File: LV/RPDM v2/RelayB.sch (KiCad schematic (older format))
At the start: 6 parts, among them K2 G8NW, Q2 Q_Dual_NMOS

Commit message: rPDM - Started on board layout
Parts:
- D6, D7: renamed from D?; footprint (none) -> Diode_UOWM:TO-277_FSV10150V
- gave numbers to parts that had none: 2
- renumbered K2 to K3, Q2 to Q3
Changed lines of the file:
@@
 $EndDescr
 $Comp
-L Device2:Q_Dual_NMOS_S1G1S2G2D2D2D1D1 Q2
+L Device2:Q_Dual_NMOS_S1G1S2G2D2D2D1D1 Q3
 U 2 1 6114EE63
 P 5900 4500
-AR Path="/5E554D5D/60DE88EB/6114EE63" Ref="Q2"  Part="2"
-AR Path="/5E554D5D/60DEDCB5/6114EE63" Ref="Q1"  Part="2"
-F 0 "Q2" H 6188 4546 50  0000 L CNN
+AR Path="/5E554D5D/60DE88EB/6114EE63" Ref="Q3"  Part="2"
+AR Path="/5E554D5D/60DEDCB5/6114EE63" Ref="Q2"  Part="2"
+F 0 "Q3" H 6188 4546 50  0000 L CNN
 F 1 "Q_Dual_NMOS" H 6188 4455 50  0000 L CNN
 F 2 "" H 6100 4500 50  0001 C CNN
@@
 $EndComp
 $Comp
-L relay_omron:G8NW K2
+L relay_omron:G8NW K3
 U 2 1 61727FFD
 P 5500 3300
-AR Path="/5E554D5D/60DE88EB/61727FFD" Ref="K2"  Part="2"
-AR Path="/5E554D5D/60DEDCB5/61727FFD" Ref="K1"  Part="2"
-F 0 "K2" V 6081 3300 50  0000 C CNN
+AR Path="/5E554D5D/60DE88EB/61727FFD" Ref="K3"  Part="2"
+AR Path="/5E554D5D/60DEDCB5/61727FFD" Ref="K2"  Part="2"
+F 0 "K3" V 6081 3300 50  0000 C CNN
 F 1 "G8NW" V 5990 3300 50  0000 C CNN
 F 2 "" H 5900 3200 50  0001 L CNN
@@
 AR Path="/5E554D5D/60DE7B67/617E89A2" Ref="#PWR?"  Part="1"
 AR Path="/5E554D5D/60DE7FBD/617E89A2" Ref="#PWR?"  Part="1"
-AR Path="/5E554D5D/60DE88EB/617E89A2" Ref="#PWR?"  Part="1"
+AR Path="/5E554D5D/60DE88EB/617E89A2" Ref="#PWR023"  Part="1"
 AR Path="/5E554D5D/60DED789/617E89A2" Ref="#PWR?"  Part="1"
-AR Path="/5E554D5D/60DEDCB5/617E89A2" Ref="#PWR?"  Part="1"
+AR Path="/5E554D5D/60DEDCB5/617E89A2" Ref="#PWR017"  Part="1"
 AR Path="/60E5EBEF/617E89A2" Ref="#PWR?"  Part="1"
-F 0 "#PWR?" H 6000 4750 50  0001 C CNN
+F 0 "#PWR023" H 6000 4750 50  0001 C CNN
 F 1 "GND" H 6005 4827 50  0000 C CNN
 F 2 "" H 6000 5000 50  0001 C CNN
@@
 AR Path="/5E554D5D/5E5E9CA9/617E89AB" Ref="R?"  Part="1"
 AR Path="/5E554D5D/60DED789/617E89AB" Ref="R?"  Part="1"
-AR Path="/5E554D5D/60DE88EB/617E89AB" Ref="R?"  Part="1"
-AR Path="/5E554D5D/60DEDCB5/617E89AB" Ref="R?"  Part="1"
-F 0 "R?" H 5070 4796 50  0000 L CNN
+AR Path="/5E554D5D/60DE88EB/617E89AB" Ref="R16"  Part="1"
+AR Path="/5E554D5D/60DEDCB5/617E89AB" Ref="R12"  Part="1"
+F 0 "R16" H 5070 4796 50  0000 L CNN
 F 1 "100k" H 5070 4705 50  0000 L CNN
 F 2 "Resistor_SMD:R_0805_2012Metric_Pad1.15x1.40mm_HandSolder" V 4930 4750 50  0001 C CNN
@@
 AR Path="/5E554D5D/60DE7B67/617E89B2" Ref="#PWR?"  Part="1"
 AR Path="/5E554D5D/60DE7FBD/617E89B2" Ref="#PWR?"  Part="1"
-AR Path="/5E554D5D/60DE88EB/617E89B2" Ref="#PWR?"  Part="1"
+AR Path="/5E554D5D/60DE88EB/617E89B2" Ref="#PWR022"  Part="1"
 AR Path="/5E554D5D/60DED789/617E89B2" Ref="#PWR?"  Part="1"
-AR Path="/5E554D5D/60DEDCB5/617E89B2" Ref="#PWR?"  Part="1"
+AR Path="/5E554D5D/60DEDCB5/617E89B2" Ref="#PWR016"  Part="1"
 AR Path="/60E5EBEF/617E89B2" Ref="#PWR?"  Part="1"
-F 0 "#PWR?" H 5000 4750 50  0001 C CNN
+F 0 "#PWR022" H 5000 4750 50  0001 C CNN
 F 1 "GND" H 5005 4827 50  0000 C CNN
 F 2 "" H 5000 5000 50  0001 C CNN
@@
 AR Path="/5E554D5D/5E5E9CA9/617E89C5" Ref="R?"  Part="1"
 AR Path="/5E554D5D/60DED789/617E89C5" Ref="R?"  Part="1"
-F 0 "R?" V 5293 4500 50  0000 C CNN
+AR Path="/5E554D5D/60DEDCB5/617E89C5" Ref="R13"  Part="1"
+AR Path="/5E554D5D/60DE88EB/617E89C5" Ref="R17"  Part="1"
+F 0 "R17" V 5293 4500 50  0000 C CNN
 F 1 "470" V 5384 4500 50  0000 C CNN
 F 2 "Resistor_SMD:R_0805_2012Metric_Pad1.15x1.40mm_HandSolder" V 5430 4500 50  0001 C CNN
@@
 AR Path="/5E554D5D/60DE7B67/617E89CB" Ref="#PWR?"  Part="1"
 AR Path="/5E554D5D/60DE7FBD/617E89CB" Ref="#PWR?"  Part="1"
-AR Path="/5E554D5D/60DE88EB/617E89CB" Ref="#PWR?"  Part="1"
+AR Path="/5E554D5D/60DE88EB/617E89CB" Ref="#PWR024"  Part="1"
 AR Path="/5E554D5D/60DED789/617E89CB" Ref="#PWR?"  Part="1"
-AR Path="/5E554D5D/60DEDCB5/617E89CB" Ref="#PWR?"  Part="1"
+AR Path="/5E554D5D/60DEDCB5/617E89CB" Ref="#PWR018"  Part="1"
 AR Path="/60E5EBEF/617E89CB" Ref="#PWR?"  Part="1"
-F 0 "#PWR?" H 6500 3750 50  0001 C CNN
+F 0 "#PWR024" H 6500 3750 50  0001 C CNN
 F 1 "GND" H 6505 3827 50  0000 C CNN
 F 2 "" H 6500 4000 50  0001 C CNN
@@
 AR Path="/5E554D5D/60DED789/617E89D1" Ref="D?"  Part="1"
 AR Path="/5E554D5D/5E5E9CA9/617E89D1" Ref="D?"  Part="1"
-F 0 "D?" H 5500 4100 50  0000 C CNN
+AR Path="/5E554D5D/60DEDCB5/617E89D1" Ref="D6"  Part="1"
+AR Path="/5E554D5D/60DE88EB/617E89D1" Ref="D10"  Part="1"
+F 0 "D10" H 5500 4100 50  0000 C CNN
 F 1 "D_Schottky_Flyback" H 5450 3900 50  0000 C CNN
-F 2 "" H 5500 4000 50  0001 C CNN
+F 2 "Diode_UOWM:TO-277_FSV10150V" H 5500 4000 50  0001 C CNN
 F 3 "~" H 5500 4000 50  0001 C CNN
 	1    5500 4000
@@
 AR Path="/5E554D5D/60DED789/617E89D7" Ref="D?"  Part="1"
 AR Path="/5E554D5D/5E5E9CA9/617E89D7" Ref="D?"  Part="1"
-F 0 "D?" V 6479 3644 50  0000 L CNN
+AR Path="/5E554D5D/60DEDCB5/617E89D7" Ref="D7"  Part="1"
+AR Path="/5E554D5D/60DE88EB/617E89D7" Ref="D11"  Part="1"
+F 0 "D11" V 6479 3644 50  0000 L CNN
 F 1 "D_Schottky_Flyback" V 6570 3644 50  0000 L CNN
-F 2 "" H 6500 3500 50  0001 C CNN
+F 2 "Diode_UOWM:TO-277_FSV10150V" H 6500 3500 50  0001 C CNN
 F 3 "~" H 6500 3500 50  0001 C CNN
 	1    6500 3500

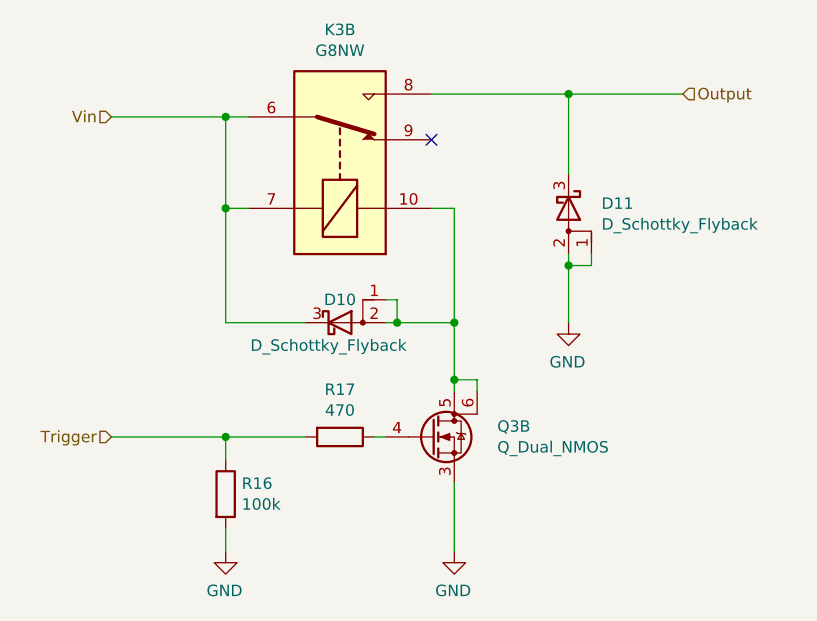
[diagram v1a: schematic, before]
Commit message: rpdm, libraries cleanup
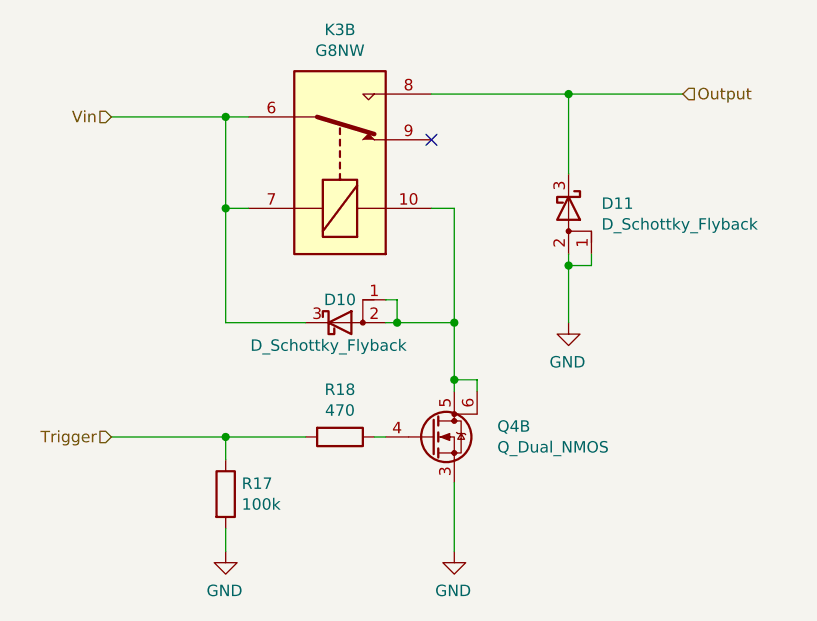
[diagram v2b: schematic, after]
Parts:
- renumbered Q3 to Q4, R13 to R14, R16 to R17
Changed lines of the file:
@@
 $EndDescr
 $Comp
-L Device2:Q_Dual_NMOS_S1G1S2G2D2D2D1D1 Q3
+L Device2:Q_Dual_NMOS_S1G1S2G2D2D2D1D1 Q4
 U 2 1 6114EE63
 P 5900 4500
-AR Path="/5E554D5D/60DE88EB/6114EE63" Ref="Q3"  Part="2"
-AR Path="/5E554D5D/60DEDCB5/6114EE63" Ref="Q2"  Part="2"
-F 0 "Q3" H 6188 4546 50  0000 L CNN
+AR Path="/5E554D5D/60DE88EB/6114EE63" Ref="Q4"  Part="2"
+AR Path="/5E554D5D/60DEDCB5/6114EE63" Ref="Q3"  Part="2"
+F 0 "Q4" H 6188 4546 50  0000 L CNN
 F 1 "Q_Dual_NMOS" H 6188 4455 50  0000 L CNN
 F 2 "" H 6100 4500 50  0001 C CNN
@@
 AR Path="/5E554D5D/5E5E9CA9/617E89AB" Ref="R?"  Part="1"
 AR Path="/5E554D5D/60DED789/617E89AB" Ref="R?"  Part="1"
-AR Path="/5E554D5D/60DE88EB/617E89AB" Ref="R16"  Part="1"
-AR Path="/5E554D5D/60DEDCB5/617E89AB" Ref="R12"  Part="1"
-F 0 "R16" H 5070 4796 50  0000 L CNN
+AR Path="/5E554D5D/60DE88EB/617E89AB" Ref="R17"  Part="1"
+AR Path="/5E554D5D/60DEDCB5/617E89AB" Ref="R13"  Part="1"
+F 0 "R17" H 5070 4796 50  0000 L CNN
 F 1 "100k" H 5070 4705 50  0000 L CNN
 F 2 "Resistor_SMD:R_0805_2012Metric_Pad1.15x1.40mm_HandSolder" V 4930 4750 50  0001 C CNN
@@
 AR Path="/5E554D5D/5E5E9CA9/617E89C5" Ref="R?"  Part="1"
 AR Path="/5E554D5D/60DED789/617E89C5" Ref="R?"  Part="1"
-AR Path="/5E554D5D/60DEDCB5/617E89C5" Ref="R13"  Part="1"
-AR Path="/5E554D5D/60DE88EB/617E89C5" Ref="R17"  Part="1"
-F 0 "R17" V 5293 4500 50  0000 C CNN
+AR Path="/5E554D5D/60DEDCB5/617E89C5" Ref="R14"  Part="1"
+AR Path="/5E554D5D/60DE88EB/617E89C5" Ref="R18"  Part="1"
+F 0 "R18" V 5293 4500 50  0000 C CNN
 F 1 "470" V 5384 4500 50  0000 C CNN
 F 2 "Resistor_SMD:R_0805_2012Metric_Pad1.15x1.40mm_HandSolder" V 5430 4500 50  0001 C CNN

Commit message: RPDM
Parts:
- D3: renamed from D6; footprint Diode_UOWM:TO-277_FSV10150V -> UOWM_Diodes:TO-277_FSV10150V
- D4: renamed from D7; footprint Diode_UOWM:TO-277_FSV10150V -> UOWM_Diodes:TO-277_FSV10150V
- K2: renamed from K3; footprint (none) -> UOWM_Relays:Omron-G8NW-2L-AS_SK-MFG
- Q3: renamed from Q4; footprint (none) -> UOWM_Package_SO:Diodes_SO-8_5.3x6.2mm_P1.27mm
- renumbered R14 to R11, R17 to R14
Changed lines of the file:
@@
 $Descr A4 11693 8268
 encoding utf-8
-Sheet 28 32
+Sheet 5 30
 Title "Relay Circuit"
 Date "2021-06-28"
@@
 $EndDescr
 $Comp
-L Device2:Q_Dual_NMOS_S1G1S2G2D2D2D1D1 Q4
+L Device2:Q_Dual_NMOS_S1G1S2G2D2D2D1D1 Q3
 U 2 1 6114EE63
 P 5900 4500
-AR Path="/5E554D5D/60DE88EB/6114EE63" Ref="Q4"  Part="2"
-AR Path="/5E554D5D/60DEDCB5/6114EE63" Ref="Q3"  Part="2"
-F 0 "Q4" H 6188 4546 50  0000 L CNN
+AR Path="/5E554D5D/60DE88EB/6114EE63" Ref="Q3"  Part="2"
+AR Path="/5E554D5D/60DEDCB5/6114EE63" Ref="Q2"  Part="2"
+F 0 "Q2" H 6188 4546 50  0000 L CNN
 F 1 "Q_Dual_NMOS" H 6188 4455 50  0000 L CNN
-F 2 "" H 6100 4500 50  0001 C CNN
-F 3 "~" H 6100 4500 50  0001 C CNN
+F 2 "UOWM_Package_SO:Diodes_SO-8_5.3x6.2mm_P1.27mm" H 6100 4500 50  0001 C CNN
+F 3 "https://www.diodes.com/assets/Datasheets/DMT3020LSDQ.pdf" H 6100 4500 50  0001 C CNN
 	2    5900 4500
 	1    0    0    -1
 $EndComp
 $Comp
-L relay_omron:G8NW K3
+L relay_omron:G8NW K2
 U 2 1 61727FFD
 P 5500 3300
-AR Path="/5E554D5D/60DE88EB/61727FFD" Ref="K3"  Part="2"
-AR Path="/5E554D5D/60DEDCB5/61727FFD" Ref="K2"  Part="2"
-F 0 "K3" V 6081 3300 50  0000 C CNN
+AR Path="/5E554D5D/60DE88EB/61727FFD" Ref="K2"  Part="2"
+AR Path="/5E554D5D/60DEDCB5/61727FFD" Ref="K1"  Part="2"
+F 0 "K1" V 6081 3300 50  0000 C CNN
 F 1 "G8NW" V 5990 3300 50  0000 C CNN
-F 2 "" H 5900 3200 50  0001 L CNN
+F 2 "UOWM_Relays:Omron-G8NW-2L-AS_SK-MFG" H 5900 3200 50  0001 L CNN
 F 3 "https://omronfs.omron.com/en_US/ecb/products/pdf/en-g8nw.pdf" H 5900 3400 50  0001 C CNN
 	2    5500 3300
@@
 AR Path="/5E554D5D/60DE7B67/617E89A2" Ref="#PWR?"  Part="1"
 AR Path="/5E554D5D/60DE7FBD/617E89A2" Ref="#PWR?"  Part="1"
-AR Path="/5E554D5D/60DE88EB/617E89A2" Ref="#PWR023"  Part="1"
+AR Path="/5E554D5D/60DE88EB/617E89A2" Ref="#PWR020"  Part="1"
 AR Path="/5E554D5D/60DED789/617E89A2" Ref="#PWR?"  Part="1"
-AR Path="/5E554D5D/60DEDCB5/617E89A2" Ref="#PWR017"  Part="1"
+AR Path="/5E554D5D/60DEDCB5/617E89A2" Ref="#PWR014"  Part="1"
 AR Path="/60E5EBEF/617E89A2" Ref="#PWR?"  Part="1"
-F 0 "#PWR023" H 6000 4750 50  0001 C CNN
+F 0 "#PWR020" H 6000 4750 50  0001 C CNN
 F 1 "GND" H 6005 4827 50  0000 C CNN
 F 2 "" H 6000 5000 50  0001 C CNN
@@
 AR Path="/5E554D5D/5E5E9CA9/617E89AB" Ref="R?"  Part="1"
 AR Path="/5E554D5D/60DED789/617E89AB" Ref="R?"  Part="1"
-AR Path="/5E554D5D/60DE88EB/617E89AB" Ref="R17"  Part="1"
-AR Path="/5E554D5D/60DEDCB5/617E89AB" Ref="R13"  Part="1"
-F 0 "R17" H 5070 4796 50  0000 L CNN
+AR Path="/5E554D5D/60DE88EB/617E89AB" Ref="R14"  Part="1"
+AR Path="/5E554D5D/60DEDCB5/617E89AB" Ref="R10"  Part="1"
+F 0 "R10" H 5070 4796 50  0000 L CNN
 F 1 "100k" H 5070 4705 50  0000 L CNN
 F 2 "Resistor_SMD:R_0805_2012Metric_Pad1.15x1.40mm_HandSolder" V 4930 4750 50  0001 C CNN
-F 3 "~" H 5000 4750 50  0001 C CNN
+F 3 "https://www.koaspeer.com/pdfs/RK73H.pdf" H 5000 4750 50  0001 C CNN
 	1    5000 4750
 	1    0    0    -1
@@
 AR Path="/5E554D5D/60DE7B67/617E89B2" Ref="#PWR?"  Part="1"
 AR Path="/5E554D5D/60DE7FBD/617E89B2" Ref="#PWR?"  Part="1"
-AR Path="/5E554D5D/60DE88EB/617E89B2" Ref="#PWR022"  Part="1"
+AR Path="/5E554D5D/60DE88EB/617E89B2" Ref="#PWR019"  Part="1"
 AR Path="/5E554D5D/60DED789/617E89B2" Ref="#PWR?"  Part="1"
-AR Path="/5E554D5D/60DEDCB5/617E89B2" Ref="#PWR016"  Part="1"
+AR Path="/5E554D5D/60DEDCB5/617E89B2" Ref="#PWR013"  Part="1"
 AR Path="/60E5EBEF/617E89B2" Ref="#PWR?"  Part="1"
-F 0 "#PWR022" H 5000 4750 50  0001 C CNN
+F 0 "#PWR019" H 5000 4750 50  0001 C CNN
 F 1 "GND" H 5005 4827 50  0000 C CNN
 F 2 "" H 5000 5000 50  0001 C CNN
@@
 AR Path="/5E554D5D/5E5E9CA9/617E89C5" Ref="R?"  Part="1"
 AR Path="/5E554D5D/60DED789/617E89C5" Ref="R?"  Part="1"
-AR Path="/5E554D5D/60DEDCB5/617E89C5" Ref="R14"  Part="1"
-AR Path="/5E554D5D/60DE88EB/617E89C5" Ref="R18"  Part="1"
-F 0 "R18" V 5293 4500 50  0000 C CNN
+AR Path="/5E554D5D/60DEDCB5/617E89C5" Ref="R11"  Part="1"
+AR Path="/5E554D5D/60DE88EB/617E89C5" Ref="R15"  Part="1"
+F 0 "R11" V 5293 4500 50  0000 C CNN
 F 1 "470" V 5384 4500 50  0000 C CNN
 F 2 "Resistor_SMD:R_0805_2012Metric_Pad1.15x1.40mm_HandSolder" V 5430 4500 50  0001 C CNN
@@
 AR Path="/5E554D5D/60DE7B67/617E89CB" Ref="#PWR?"  Part="1"
 AR Path="/5E554D5D/60DE7FBD/617E89CB" Ref="#PWR?"  Part="1"
-AR Path="/5E554D5D/60DE88EB/617E89CB" Ref="#PWR024"  Part="1"
+AR Path="/5E554D5D/60DE88EB/617E89CB" Ref="#PWR021"  Part="1"
 AR Path="/5E554D5D/60DED789/617E89CB" Ref="#PWR?"  Part="1"
-AR Path="/5E554D5D/60DEDCB5/617E89CB" Ref="#PWR018"  Part="1"
+AR Path="/5E554D5D/60DEDCB5/617E89CB" Ref="#PWR015"  Part="1"
 AR Path="/60E5EBEF/617E89CB" Ref="#PWR?"  Part="1"
-F 0 "#PWR024" H 6500 3750 50  0001 C CNN
+F 0 "#PWR021" H 6500 3750 50  0001 C CNN
 F 1 "GND" H 6505 3827 50  0000 C CNN
 F 2 "" H 6500 4000 50  0001 C CNN
@@
 AR Path="/5E554D5D/60DED789/617E89D1" Ref="D?"  Part="1"
 AR Path="/5E554D5D/5E5E9CA9/617E89D1" Ref="D?"  Part="1"
-AR Path="/5E554D5D/60DEDCB5/617E89D1" Ref="D6"  Part="1"
-AR Path="/5E554D5D/60DE88EB/617E89D1" Ref="D10"  Part="1"
-F 0 "D10" H 5500 4100 50  0000 C CNN
+AR Path="/5E554D5D/60DEDCB5/617E89D1" Ref="D3"  Part="1"
+AR Path="/5E554D5D/60DE88EB/617E89D1" Ref="D7"  Part="1"
+F 0 "D3" H 5500 4100 50  0000 C CNN
 F 1 "D_Schottky_Flyback" H 5450 3900 50  0000 C CNN
-F 2 "Diode_UOWM:TO-277_FSV10150V" H 5500 4000 50  0001 C CNN
+F 2 "UOWM_Diodes:TO-277_FSV10150V" H 5500 4000 50  0001 C CNN
 F 3 "~" H 5500 4000 50  0001 C CNN
 	1    5500 4000
@@
 AR Path="/5E554D5D/60DED789/617E89D7" Ref="D?"  Part="1"
 AR Path="/5E554D5D/5E5E9CA9/617E89D7" Ref="D?"  Part="1"
-AR Path="/5E554D5D/60DEDCB5/617E89D7" Ref="D7"  Part="1"
-AR Path="/5E554D5D/60DE88EB/617E89D7" Ref="D11"  Part="1"
-F 0 "D11" V 6479 3644 50  0000 L CNN
+AR Path="/5E554D5D/60DEDCB5/617E89D7" Ref="D4"  Part="1"
+AR Path="/5E554D5D/60DE88EB/617E89D7" Ref="D8"  Part="1"
+F 0 "D4" V 6479 3644 50  0000 L CNN
 F 1 "D_Schottky_Flyback" V 6570 3644 50  0000 L CNN
-F 2 "Diode_UOWM:TO-277_FSV10150V" H 6500 3500 50  0001 C CNN
+F 2 "UOWM_Diodes:TO-277_FSV10150V" H 6500 3500 50  0001 C CNN
 F 3 "~" H 6500 3500 50  0001 C CNN
 	1    6500 3500

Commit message: RPDM
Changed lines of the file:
@@
 $Descr A4 11693 8268
 encoding utf-8
-Sheet 28 30
+Sheet 30 30
 Title "Relay Circuit"
 Date "2021-06-28"
@@
 AR Path="/5E554D5D/60DE88EB/6114EE63" Ref="Q3"  Part="2"
 AR Path="/5E554D5D/60DEDCB5/6114EE63" Ref="Q2"  Part="2"
-F 0 "Q2" H 6188 4546 50  0000 L CNN
+F 0 "Q3" H 6188 4546 50  0000 L CNN
 F 1 "Q_Dual_NMOS" H 6188 4455 50  0000 L CNN
 F 2 "UOWM_Package_SO:Diodes_SO-8_5.3x6.2mm_P1.27mm" H 6100 4500 50  0001 C CNN
@@
 AR Path="/5E554D5D/60DE88EB/61727FFD" Ref="K2"  Part="2"
 AR Path="/5E554D5D/60DEDCB5/61727FFD" Ref="K1"  Part="2"
-F 0 "K1" V 6081 3300 50  0000 C CNN
+F 0 "K2" V 6081 3300 50  0000 C CNN
 F 1 "G8NW" V 5990 3300 50  0000 C CNN
 F 2 "UOWM_Relays:Omron-G8NW-2L-AS_SK-MFG" H 5900 3200 50  0001 L CNN
@@
 AR Path="/5E554D5D/60DEDCB5/617E89A2" Ref="#PWR014"  Part="1"
 AR Path="/60E5EBEF/617E89A2" Ref="#PWR?"  Part="1"
-F 0 "#PWR014" H 6000 4750 50  0001 C CNN
+F 0 "#PWR020" H 6000 4750 50  0001 C CNN
 F 1 "GND" H 6005 4827 50  0000 C CNN
 F 2 "" H 6000 5000 50  0001 C CNN
@@
 AR Path="/5E554D5D/60DE88EB/617E89AB" Ref="R14"  Part="1"
 AR Path="/5E554D5D/60DEDCB5/617E89AB" Ref="R10"  Part="1"
-F 0 "R10" H 5070 4796 50  0000 L CNN
+F 0 "R14" H 5070 4796 50  0000 L CNN
 F 1 "100k" H 5070 4705 50  0000 L CNN
 F 2 "Resistor_SMD:R_0805_2012Metric_Pad1.15x1.40mm_HandSolder" V 4930 4750 50  0001 C CNN
@@
 AR Path="/5E554D5D/60DEDCB5/617E89B2" Ref="#PWR013"  Part="1"
 AR Path="/60E5EBEF/617E89B2" Ref="#PWR?"  Part="1"
-F 0 "#PWR013" H 5000 4750 50  0001 C CNN
+F 0 "#PWR019" H 5000 4750 50  0001 C CNN
 F 1 "GND" H 5005 4827 50  0000 C CNN
 F 2 "" H 5000 5000 50  0001 C CNN
@@
 AR Path="/5E554D5D/60DEDCB5/617E89C5" Ref="R11"  Part="1"
 AR Path="/5E554D5D/60DE88EB/617E89C5" Ref="R15"  Part="1"
-F 0 "R11" V 5293 4500 50  0000 C CNN
+F 0 "R15" V 5293 4500 50  0000 C CNN
 F 1 "470" V 5384 4500 50  0000 C CNN
 F 2 "Resistor_SMD:R_0805_2012Metric_Pad1.15x1.40mm_HandSolder" V 5430 4500 50  0001 C CNN
@@
 AR Path="/5E554D5D/60DEDCB5/617E89CB" Ref="#PWR015"  Part="1"
 AR Path="/60E5EBEF/617E89CB" Ref="#PWR?"  Part="1"
-F 0 "#PWR015" H 6500 3750 50  0001 C CNN
+F 0 "#PWR021" H 6500 3750 50  0001 C CNN
 F 1 "GND" H 6505 3827 50  0000 C CNN
 F 2 "" H 6500 4000 50  0001 C CNN
@@
 AR Path="/5E554D5D/60DEDCB5/617E89D1" Ref="D3"  Part="1"
 AR Path="/5E554D5D/60DE88EB/617E89D1" Ref="D7"  Part="1"
-F 0 "D3" H 5500 4100 50  0000 C CNN
+F 0 "D7" H 5500 4100 50  0000 C CNN
 F 1 "D_Schottky_Flyback" H 5450 3900 50  0000 C CNN
 F 2 "UOWM_Diodes:TO-277_FSV10150V" H 5500 4000 50  0001 C CNN
@@
 AR Path="/5E554D5D/60DEDCB5/617E89D7" Ref="D4"  Part="1"
 AR Path="/5E554D5D/60DE88EB/617E89D7" Ref="D8"  Part="1"
-F 0 "D4" V 6479 3644 50  0000 L CNN
+F 0 "D8" V 6479 3644 50  0000 L CNN
 F 1 "D_Schottky_Flyback" V 6570 3644 50  0000 L CNN
 F 2 "UOWM_Diodes:TO-277_FSV10150V" H 6500 3500 50  0001 C CNN
